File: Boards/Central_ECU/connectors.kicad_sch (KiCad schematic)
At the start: 35 parts, among them J1 DE9_Socket, J10 SWD JST, J2 DE9_Socket, J3 RS422 JST, J4 USB_B_Micro, J5 Ignitor JST, J6 MICROFIT, J7 MICROFIT, J8 Solenoid MICROFIT, J9 Siren MICROFIT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

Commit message: Nearing completion
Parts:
- added D8: PESD3V3L4UW, Package_TO_SOT_SMD:SOT-665, symbol Power_Protection:PESD3V3L4UW
- added D9: D_TVS, symbol Device:D_TVS
- added J12: UART JST, symbol Connector_Generic:Conn_01x03
- added J13: I2CA JST, symbol Connector_Generic:Conn_01x05
- added J14: I2CB JST, symbol Connector_Generic:Conn_01x05
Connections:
- net +7V4: now also R33.1, J13.5 (Pin_5), J14.5 (Pin_5)
- net 4S_V+: now also D7.2 (A), SW1.2 (Pin_2), D9.2 (A2); no longer D5.1 (K), Q4.3 (S)
- net GND: now also D8.2 (A), D9.1 (A1), J12.2 (Pin_2), J13.1 (Pin_1), J14.1 (Pin_1)
- net at D7.1 (K), R31.1, SW1.1 (Pin_1): now also D5.1 (K), Q4.3 (S); no longer F2.2
- net at D3.2 (A2), Q4.1 (D): now also F2.2; no longer D7.2 (A), SW1.2 (Pin_2)
- net at F3.2, SW2.1 (Pin_1): no longer R33.1
- new net I2CA_SCL: D8.5 (K4), J13.4 (Pin_4)
- new net I2CA_SDA: D8.4 (K3), J13.2 (Pin_2)
- new net I2CB_SCL: D8.3 (K2), J14.4 (Pin_4)
- new net I2CB_SDA: D8.1 (K1), J14.2 (Pin_2)
- new net UART_RX: J12.1 (Pin_1)
- new net UART_TX: J12.3 (Pin_3)
- no-connect marks 6 -> 8
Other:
- note added: "I^{2}C"
- note added: "UART"
- note removed: "TODO: Add I2C interfaces Add SPI interface Connector for external LED?"
- moved on the sheet: D3, D5, D7, J10, J4, Q4, R11, R31, R32, R33, R34, SW1

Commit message: For review
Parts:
- removed Q4, Q5: PMOS, symbol Simulation_SPICE:PMOS
- added J2: Extras JST, Connector_JST:JST_PH_B7B-PH-K_1x07_P2.00mm_Vertical, symbol Connector_Generic:Conn_01x07
- added Q4, Q5: DMP6023LFG, Package_SON:Diodes_PowerDI3333-8, symbol Transistor_FET:DMP3013SFV
- added R40, R41, R42: 0R, Resistor_SMD:R_0805_2012Metric, symbol Device:R
- C36: renamed from C33; footprint (none) -> Capacitor_SMD:CP_Elec_8x10.5; MPN (none) -> A768KE107M1VLAE036
- C37: renamed from C34; footprint (none) -> Capacitor_SMD:C_0805_2012Metric
- C38: renamed from C35; footprint (none) -> Capacitor_SMD:C_1206_3216Metric
- C39: renamed from C37; footprint (none) -> Capacitor_SMD:C_0805_2012Metric
- C40: renamed from C36; footprint (none) -> Capacitor_SMD:C_1206_3216Metric
- C41: renamed from C32; footprint (none) -> Capacitor_SMD:CP_Elec_8x10.5; MPN (none) -> A768KE107M1VLAE036
- D10: renamed from D9; value D_TVS -> 30V 34VC; footprint (none) -> Diode_SMD:D_SOD-882; MPN (none) -> PESD1CANFD30L-QYL
- D11: renamed from D7; footprint (none) -> Diode_SMD:D_SOD-882; MPN (none) -> CTS05S40,L3F
- D13: renamed from D4; value D_TVS -> 9V 15.4VC; footprint (none) -> Diode_SMD:D_SOD-123F; MPN (none) -> SMF9.0CA
- D14: renamed from D6; value D_Zener -> 18V; footprint (none) -> Diode_SMD:D_SOD-323F; MPN (none) -> MM3Z18VB
- D8: renamed from D3; value D_TVS -> 30V 34VC; footprint (none) -> Diode_SMD:D_SOD-882; MPN (none) -> PESD1CANFD30L-QYL
- D9: renamed from D5; value D_Zener -> 18V; footprint (none) -> Diode_SMD:D_SOD-323F; MPN (none) -> MM3Z18VB
- F2: value Fuse -> 4A; footprint (none) -> Fuse:Fuse_1206_3216Metric
- F3: value Fuse -> 5A; footprint (none) -> Fuse:Fuse_1206_3216Metric
- J10: renamed from J8; value Solenoid MICROFIT -> Solenoid NANOFIT; footprint (none) -> Connector_Molex:Molex_Nano-Fit_105309-xx02_1x02_P2.50mm_Vertical; MPN (none) -> 1053091102
- J11: renamed from J2; value DE9_Socket -> DB9 Microfit; footprint (none) -> Connector_Molex:Molex_Micro-Fit_3.0_43045-1012_2x05_P3.00mm_Vertical; MPN (none) -> 0430451027
- J12: renamed from J3; footprint (none) -> Connector_JST:JST_PH_B6B-PH-K_1x06_P2.00mm_Vertical; MPN (none) -> B6B-PH-K-S
- J13: renamed from J4; footprint (none) -> Connector_USB:USB_Micro-B_Amphenol_10118193-0001LF_Horizontal; MPN (none) -> 10118193-0001LF
- J14: renamed from J10; footprint (none) -> Connector_JST:JST_PH_B3B-PH-K_1x03_P2.00mm_Vertical; MPN (none) -> B3B-PH-K-S
- J15: renamed from J12; footprint (none) -> Connector_JST:JST_PH_B3B-PH-K_1x03_P2.00mm_Vertical; MPN (none) -> B3B-PH-K-S
- J3: renamed from J6; footprint (none) -> Connector_Molex:Molex_Micro-Fit_3.0_43045-0412_2x02_P3.00mm_Vertical; MPN (none) -> 0430450412
- J4: renamed from J9; footprint (none) -> Connector_Molex:Molex_Micro-Fit_3.0_43650-0315_1x03_P3.00mm_Vertical; MPN (none) -> 436500315
- J5: renamed from J14; footprint (none) -> Connector_JST:JST_PH_B5B-PH-K_1x05_P2.00mm_Vertical; MPN (none) -> B6B-PH-K-S
- J6: renamed from J7; footprint (none) -> Connector_Molex:Molex_Micro-Fit_3.0_43045-0412_2x02_P3.00mm_Vertical; MPN (none) -> 430450412
- J7: renamed from J13; footprint (none) -> Connector_JST:JST_PH_B5B-PH-K_1x05_P2.00mm_Vertical; MPN (none) -> B5B-PH-K-S
- J8: renamed from J5; footprint (none) -> Connector_JST:JST_EH_B4B-EH-A_1x04_P2.50mm_Vertical; MPN (none) -> B4B-PH-K-S
- J9: renamed from J1; value DE9_Socket -> DB9 MICROFIT; footprint (none) -> Connector_Molex:Molex_Micro-Fit_3.0_43045-1012_2x05_P3.00mm_Vertical; MPN (none) -> 0430451027
- R43: renamed from R11; value R -> 100K; footprint (none) -> Resistor_SMD:R_0805_2012Metric
- R44: renamed from R31; footprint (none) -> Resistor_SMD:R_0805_2012Metric
- R45: renamed from R32; footprint (none) -> Resistor_SMD:R_0805_2012Metric
- R46: renamed from R15; value R -> 100K; footprint (none) -> Resistor_SMD:R_0805_2012Metric
- R47: renamed from R33; footprint (none) -> Resistor_SMD:R_0805_2012Metric
- R48: renamed from R34; footprint (none) -> Resistor_SMD:R_0805_2012Metric
- SW1, SW2: footprint (none) -> Connector_Molex:Molex_Micro-Fit_3.0_43650-0215_1x02_P3.00mm_Vertical; MPN (none) -> 436500228
- U7: renamed from U6; footprint (none) -> Package_TO_SOT_SMD:SOT-223-3_TabPin2; MPN (none) -> AZ1117CH-5.0TRG1
- U8: renamed from U7; footprint (none) -> Package_TO_SOT_SMD:SOT-223-3_TabPin2; MPN (none) -> AZ1117CH-3.3TRG1
- renumbered D8 to D12
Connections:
- net +7V4: now also Q5.1 (S), Q5.2 (S), Q5.3 (S), R42.1; no longer J5.5 (Pin_5), J7.5 (Pin_5)
- net GND: now also J2.1 (Pin_1), J2.7 (Pin_7)
- net +5V: now reaches J5.3 (Pin_3)
- net +5V: now also J7.3 (Pin_3), R41.1
- net at D8.2 (A2), F2.2: now also Q4.5 (D)
- net at D9.2 (A), R43.1: now also Q4.4 (G)
- net at D14.2 (A), R46.1: now also Q5.4 (G)
- net at D13.2 (A2), SW2.2 (Pin_2): now also Q5.5 (D)
- net at D11.1 (K), D9.1 (K), R44.1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: now also Q4.1 (S), Q4.2 (S), Q4.3 (S)
- new net: J2.4 (Pin_4), R40.2, R41.2, R42.2
- new net +3V3: J5.5 (Pin_5), J7.5 (Pin_5), R40.1
- new net E1: J2.2 (Pin_2)
- new net E2: J2.3 (Pin_3)
- new net E3: J2.5 (Pin_5)
- new net E4: J2.6 (Pin_6)
- no-connect marks 8 -> 6
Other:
- note added: "Extras"
- note added: "Fuse values are semi arbritary, actually work out"
- company: (none) -> Hybrid Test Stand 2025
- title: (none) -> Connectors
- moved on the sheet: C36, D12A, D12B, D12C, D12D

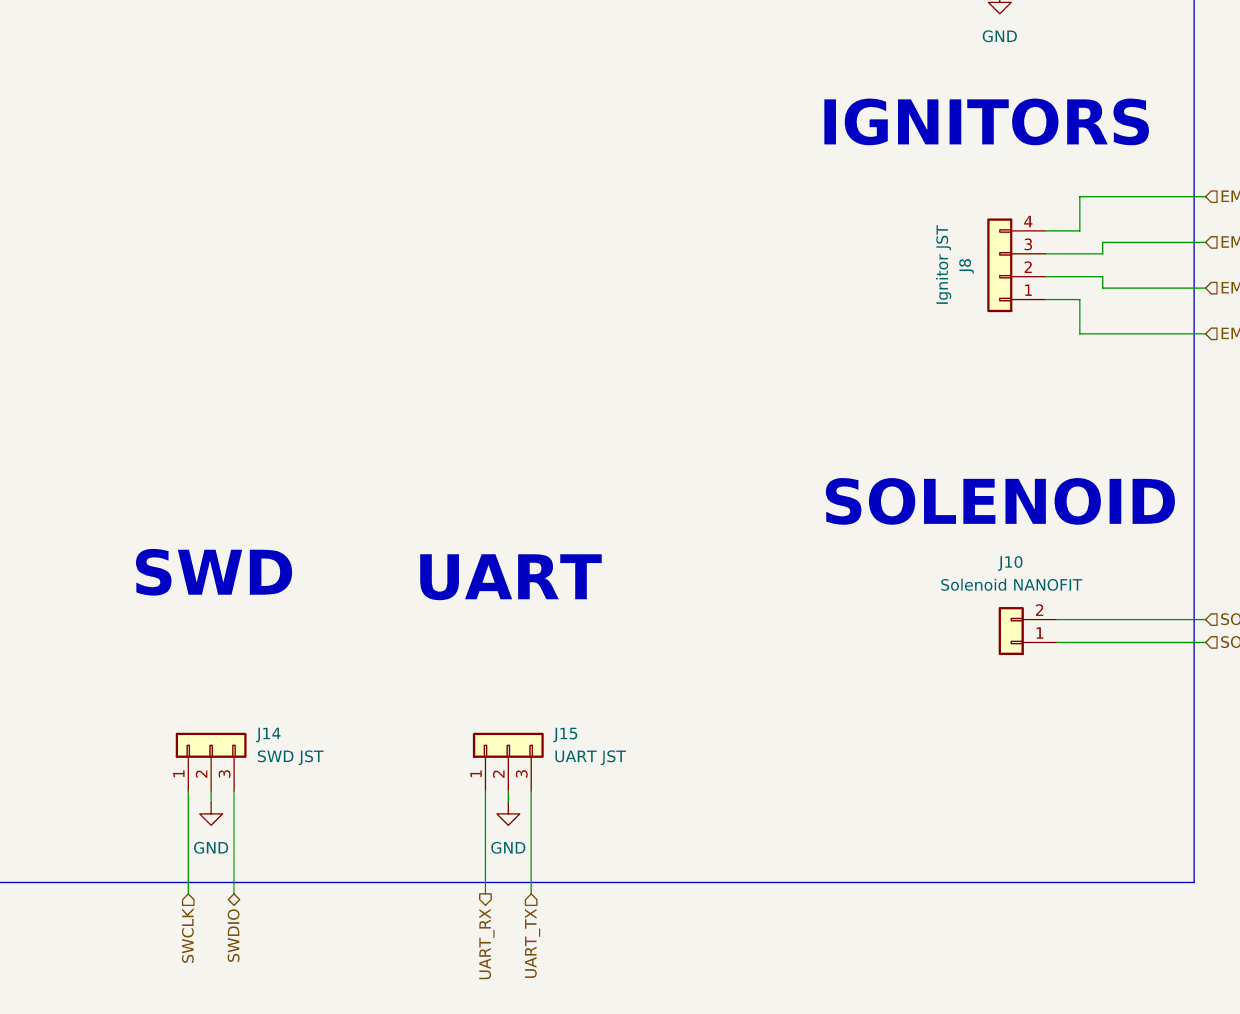
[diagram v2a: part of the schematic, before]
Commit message: Changed to 0603 passives and added NRST line
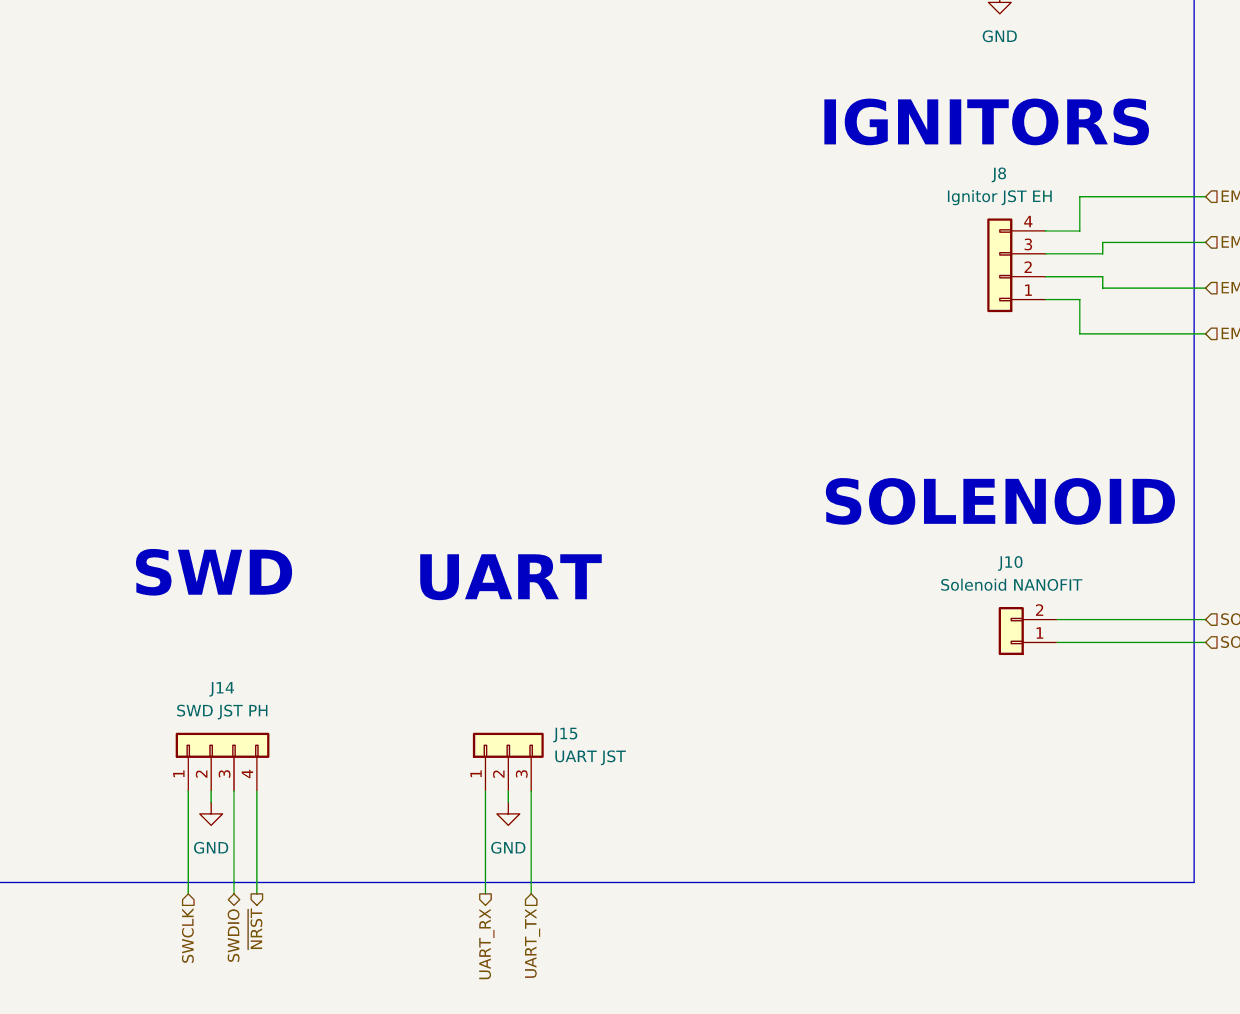
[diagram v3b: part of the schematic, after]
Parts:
- removed J14: SWD JST, Connector_JST:JST_PH_B3B-PH-K_1x03_P2.00mm_Vertical, symbol Connector_Generic:Conn_01x03
- added J14: SWD JST PH, Connector_JST:JST_PH_B4B-PH-K_1x04_P2.00mm_Vertical, symbol Connector_Generic:Conn_01x04
- C37, C39: footprint Capacitor_SMD:C_0805_2012Metric -> Capacitor_SMD:C_0603_1608Metric
- J8: value Ignitor JST -> Ignitor JST EH
- R40, R41, R42, R43, R44, R45, R46, R47, R48: footprint Resistor_SMD:R_0805_2012Metric -> Resistor_SMD:R_0603_1608Metric
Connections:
- net GND: now also J14.2 (Pin_2)
- net SWCLK: now also J14.1 (Pin_1)
- net SWDIO: now also J14.3 (Pin_3)
- new net ~{NRST}: J14.4 (Pin_4)
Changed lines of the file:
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@@
 	(wire
 		(pts
+			(xy 280.67 224.79) (xy 280.67 236.22)
+		)
+		(stroke
+			(width 0)
+			(type default)
+		)
+	)
+	(wire
+		(pts
 			(xy 139.7 49.53) (xy 144.78 49.53)
 		)
@@
 		)
 	)
+	(hierarchical_label "~{NRST}"
+		(shape output)
+		(at 280.67 236.22 270)
+		(effects
+			(font
+				(size 1.27 1.27)
+			)
+			(justify right)
+		)
+	)
 	(hierarchical_label "422_TX-"
 		(shape input)
@@
 		(fields_autoplaced yes)
 		(property "Reference" "J8"
-			(at 359.41 166.37 90)
+			(at 363.22 156.21 0)
 			(effects
 				(font
@@
 			)
 		)
-		(property "Value" "Ignitor JST"
-			(at 356.87 166.37 90)
+		(property "Value" "Ignitor JST EH"
+			(at 363.22 158.75 0)
 			(effects
 				(font
@@
 	)
 	(symbol
-		(lib_id "Connector_Generic:Conn_01x03")
-		(at 275.59 219.71 90)
-		(unit 1)
-		(exclude_from_sim no)
-		(in_bom yes)
-		(on_board yes)
-		(dnp no)
-		(fields_autoplaced yes)
-		(property "Reference" "J14"
-			(at 280.67 218.4399 90)
-			(effects
-				(font
-					(size 1.27 1.27)
-				)
-				(justify right)
-			)
-		)
-		(property "Value" "SWD JST"
-			(at 280.67 220.9799 90)
-			(effects
-				(font
-					(size 1.27 1.27)
-				)
-				(justify right)
-			)
-		)
-		(property "Footprint" "Connector_JST:JST_PH_B3B-PH-K_1x03_P2.00mm_Vertical"
-			(at 275.59 219.71 0)
-			(effects
-				(font
-					(size 1.27 1.27)
-				)
-				(hide yes)
-			)
-		)
-		(property "Datasheet" "https://www.jst-mfg.com/product/pdf/eng/ePH.pdf"
-			(at 275.59 219.71 0)
-			(effects
-				(font
-					(size 1.27 1.27)
-				)
-				(hide yes)
-			)
-		)
-		(property "Description" "Generic connector, single row, 01x03, script generated (kicad-library-utils/schlib/autogen/connector/)"
-			(at 275.59 219.71 0)
-			(effects
-				(font
-					(size 1.27 1.27)
-				)
-				(hide yes)
-			)
-		)
-		(property "MPN" "B3B-PH-K-S"
-			(at 275.59 219.71 90)
-			(effects
-				(font
-					(size 1.27 1.27)
-				)
-				(hide yes)
-			)
-		)
-		(pin "2"
-		)
-		(pin "1"
-		)
-		(pin "3"
-		)
-		(instances
-			(project ""
-				(path "/24ed8402-c9e1-4a61-8a56-11abd1b07d91/11639c01-8282-4891-a201-9121a32f140b"
-					(reference "J14")
-					(unit 1)
-				)
-			)
-		)
-	)
-	(symbol
 		(lib_id "power:+3V3")
 		(at 360.68 118.11 0)
@@
 			)
 		)
-		(property "Footprint" "Resistor_SMD:R_0805_2012Metric"
+		(property "Footprint" "Resistor_SMD:R_0603_1608Metric"
 			(at 103.632 63.5 90)
 			(effects
@@
 			)
 		)
-		(property "Footprint" "Capacitor_SMD:C_0805_2012Metric"
+		(property "Footprint" "Capacitor_SMD:C_0603_1608Metric"
 			(at 252.4252 71.12 0)
 			(effects
@@
 			)
 		)
-		(property "Footprint" "Resistor_SMD:R_0805_2012Metric"
+		(property "Footprint" "Resistor_SMD:R_0603_1608Metric"
 			(at 127.762 78.74 90)
 			(effects
@@
 			)
 		)
-		(property "Footprint" "Resistor_SMD:R_0805_2012Metric"
+		(property "Footprint" "Resistor_SMD:R_0603_1608Metric"
 			(at 141.732 106.68 90)
 			(effects
@@
 			)
 		)
-		(property "Footprint" "Resistor_SMD:R_0805_2012Metric"
+		(property "Footprint" "Resistor_SMD:R_0603_1608Metric"
 			(at 338.582 45.72 90)
 			(effects
@@
 			)
 		)
-		(property "Footprint" "Capacitor_SMD:C_0805_2012Metric"
+		(property "Footprint" "Capacitor_SMD:C_0603_1608Metric"
 			(at 215.5952 71.12 0)
 			(effects
@@
 			)
 		)
-		(property "Footprint" "Resistor_SMD:R_0805_2012Metric"
+		(property "Footprint" "Resistor_SMD:R_0603_1608Metric"
 			(at 320.802 45.72 90)
 			(effects
@@
 			)
 		)
-		(property "Footprint" "Resistor_SMD:R_0805_2012Metric"
+		(property "Footprint" "Resistor_SMD:R_0603_1608Metric"
 			(at 329.692 45.72 90)
 			(effects
@@
 			)
 		)
-		(property "Footprint" "Resistor_SMD:R_0805_2012Metric"
+		(property "Footprint" "Resistor_SMD:R_0603_1608Metric"
 			(at 127.762 71.12 90)
 			(effects
@@
 	)
 	(symbol
+		(lib_id "Connector_Generic:Conn_01x04")
+		(at 275.59 219.71 90)
+		(unit 1)
+		(exclude_from_sim no)
+		(in_bom yes)
+		(on_board yes)
+		(dnp no)
+		(fields_autoplaced yes)
+		(property "Reference" "J14"
+			(at 276.86 213.36 90)
+			(effects
+				(font
+					(size 1.27 1.27)
+				)
+			)
+		)
+		(property "Value" "SWD JST PH"
+			(at 276.86 215.9 90)
+			(effects
+				(font
+					(size 1.27 1.27)
+				)
+			)
+		)
+		(property "Footprint" "Connector_JST:JST_PH_B4B-PH-K_1x04_P2.00mm_Vertical"
+			(at 275.59 219.71 0)
+			(effects
+				(font
+					(size 1.27 1.27)
+				)
+				(hide yes)
+			)
+		)
+		(property "Datasheet" "https://www.jst-mfg.com/product/pdf/eng/ePH.pdf"
+			(at 275.59 219.71 0)
+			(effects
+				(font
+					(size 1.27 1.27)
+				)
+				(hide yes)
+			)
+		)
+		(property "Description" "Generic connector, single row, 01x04, script generated (kicad-library-utils/schlib/autogen/connector/)"
+			(at 275.59 219.71 0)
+			(effects
+				(font
+					(size 1.27 1.27)
+				)
+				(hide yes)
+			)
+		)
+		(property "MPN" "B4B-PH-K-S"
+			(at 275.59 219.71 90)
+			(effects
+				(font
+					(size 1.27 1.27)
+				)
+				(hide yes)
+			)
+		)
+		(pin "1"
+		)
+		(pin "3"
+		)
+		(pin "4"
+		)
+		(pin "2"
+		)
+		(instances
+			(project ""
+				(path "/24ed8402-c9e1-4a61-8a56-11abd1b07d91/11639c01-8282-4891-a201-9121a32f140b"
+					(reference "J14")
+					(unit 1)
+				)
+			)
+		)
+	)
+	(symbol
 		(lib_id "power:+3V3")
 		(at 68.58 162.56 0)
@@
 					(unit 1)
 				)
-				(path "/24ed8402-c9e1-4a61-8a56-11abd1b07d91/2e6b12ab-ed95-45d4-9da7-c2098bba7a10"
-					(reference "D11")
-					(unit 1)
-				)
 			)
 		)
@@
 			)
 		)
-		(property "Footprint" "Resistor_SMD:R_0805_2012Metric"
+		(property "Footprint" "Resistor_SMD:R_0603_1608Metric"
 			(at 186.182 119.38 90)
 			(effects
@@
 			)
 		)
-		(property "Footprint" "Resistor_SMD:R_0805_2012Metric"
+		(property "Footprint" "Resistor_SMD:R_0603_1608Metric"
 			(at 186.182 111.76 90)
 			(effects

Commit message: Tidy up, will send to Chris
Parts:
- D12: MPN (none) -> PESD3V3L4UW,115
- J6: MPN 430450412 -> 0430450412

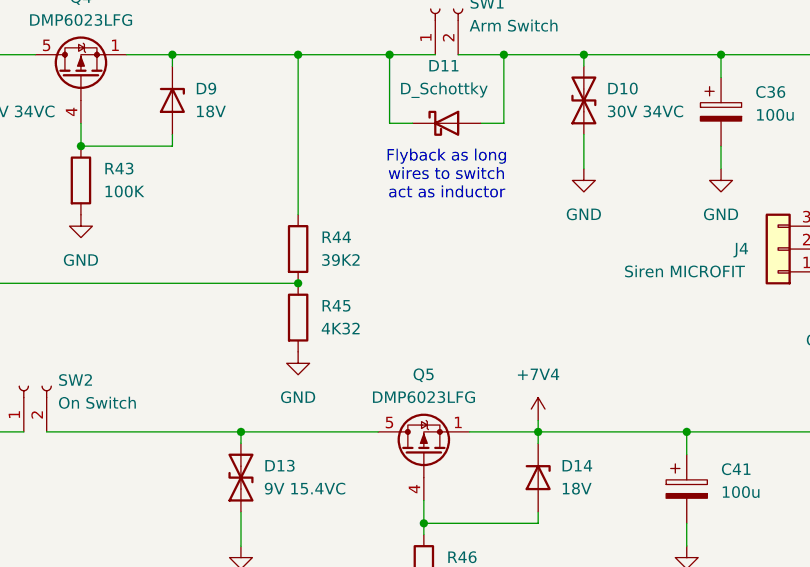
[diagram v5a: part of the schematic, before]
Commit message: Fixed voltage divider and comparator bias
Re feedback from Chris still need to fix regulator power dissipation. Happy with other points being non-issues at current.
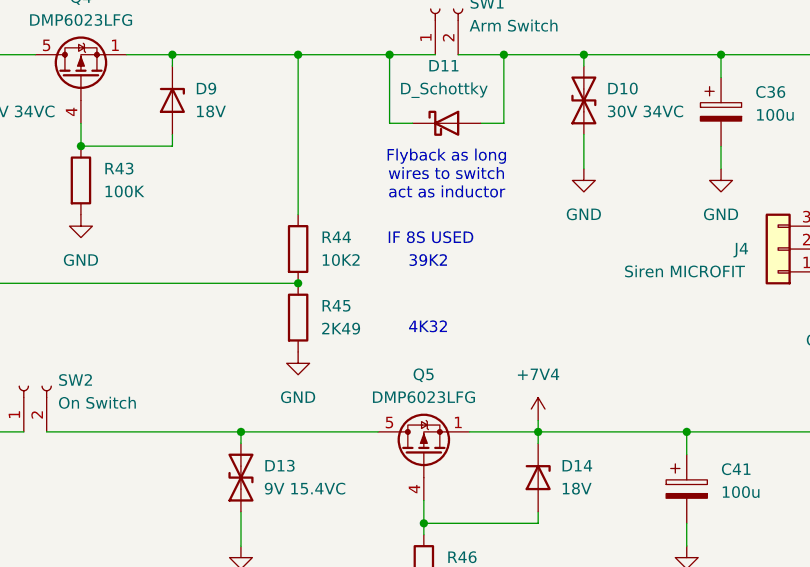
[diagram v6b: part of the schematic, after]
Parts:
- R44: value 39K2 -> 10K2
- R45: value 4K32 -> 2K49
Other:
- note added: "39K2"
- note added: "4K32"
- note added: "IF 8S USED"
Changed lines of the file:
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@@
 		)
 	)
+	(text "4K32"
+		(exclude_from_sim no)
+		(at 144.018 80.01 0)
+		(effects
+			(font
+				(size 1.27 1.27)
+			)
+		)
+	)
 	(text "4S with max voltage 16.8V, nom 14.8.\nAlso should allow for 3S (11.1V, max 12.6V)\nAnd 6-7S (22.2V, max 25.2 / 25.9, max 29.4V)\nOr regulated 24V input"
 		(exclude_from_sim no)
@@
 		)
 	)
+	(text "IF 8S USED"
+		(exclude_from_sim no)
+		(at 144.272 70.104 0)
+		(effects
+			(font
+				(size 1.27 1.27)
+			)
+		)
+	)
+	(text "39K2"
+		(exclude_from_sim no)
+		(at 144.018 72.644 0)
+		(effects
+			(font
+				(size 1.27 1.27)
+			)
+		)
+	)
 	(text "Reverse Polarity Protection"
 		(exclude_from_sim no)
@@
 			)
 		)
-		(property "Value" "4K32"
+		(property "Value" "2K49"
 			(at 132.08 80.0099 0)
 			(effects
@@
 			)
 		)
-		(property "Value" "39K2"
+		(property "Value" "10K2"
 			(at 132.08 72.3899 0)
 			(effects
